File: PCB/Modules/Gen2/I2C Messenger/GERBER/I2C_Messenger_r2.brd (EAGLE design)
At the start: 40.2 x 83 mm, 17 parts, among them IC1 SN65HVD31DR, IC2 LM3480-5.0

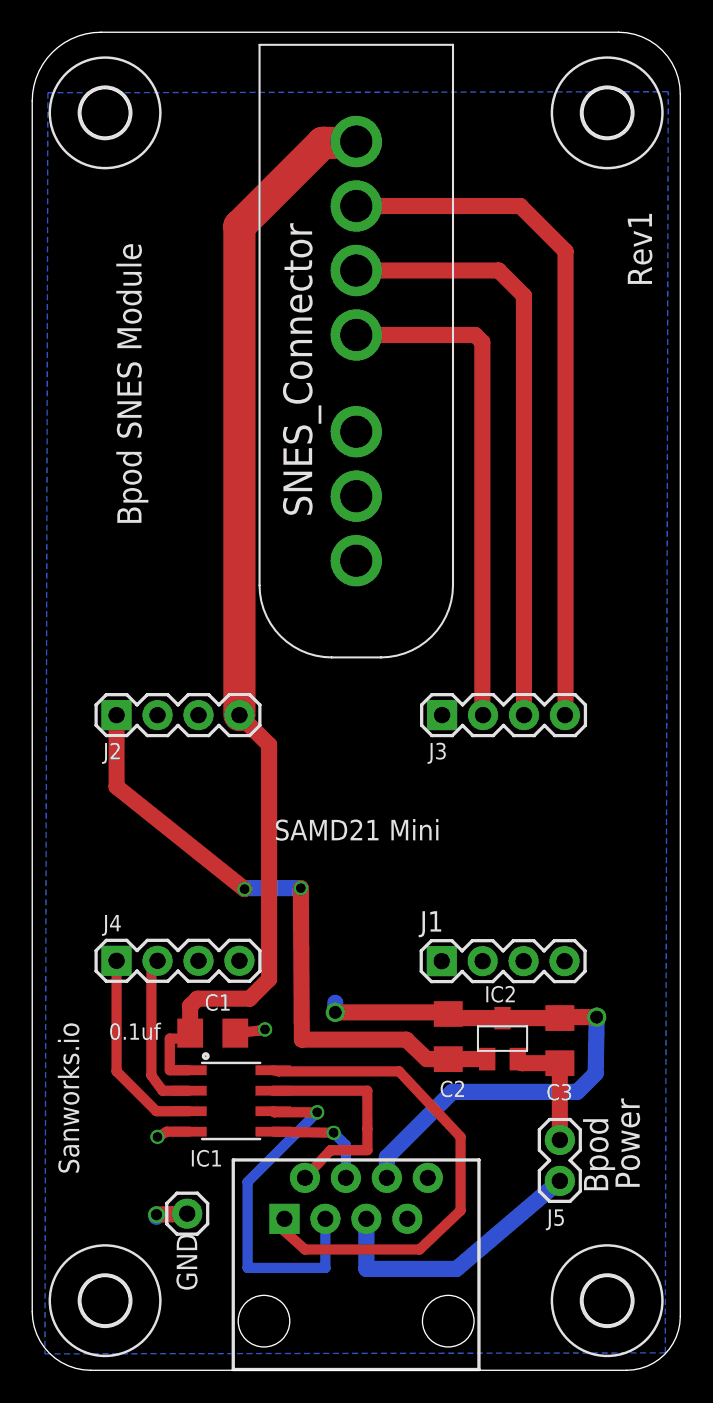
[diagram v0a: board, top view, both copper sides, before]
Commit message: -Critical Update for modules with optional RJ45 power (ValveDriver, I2C, SNES and DDS); new PCB designs add a diode to prevent USB power from entering output pin of 5V regulator, when RJ45 (state machine) power is not connected. This update greatly reduces unnecessary power consumption and heat dissipation. If you built a board using the previous designs, please Email a photo of your board to Sanworks support for a free upgrade. -Updated component names on some boards and on web BOMs to avoid skipping parts -Renamed Gen2 module PCB folder from '0.7' to 'Gen2' -Retired pocket state machine (to be replaced with Bpod State Machine r1)
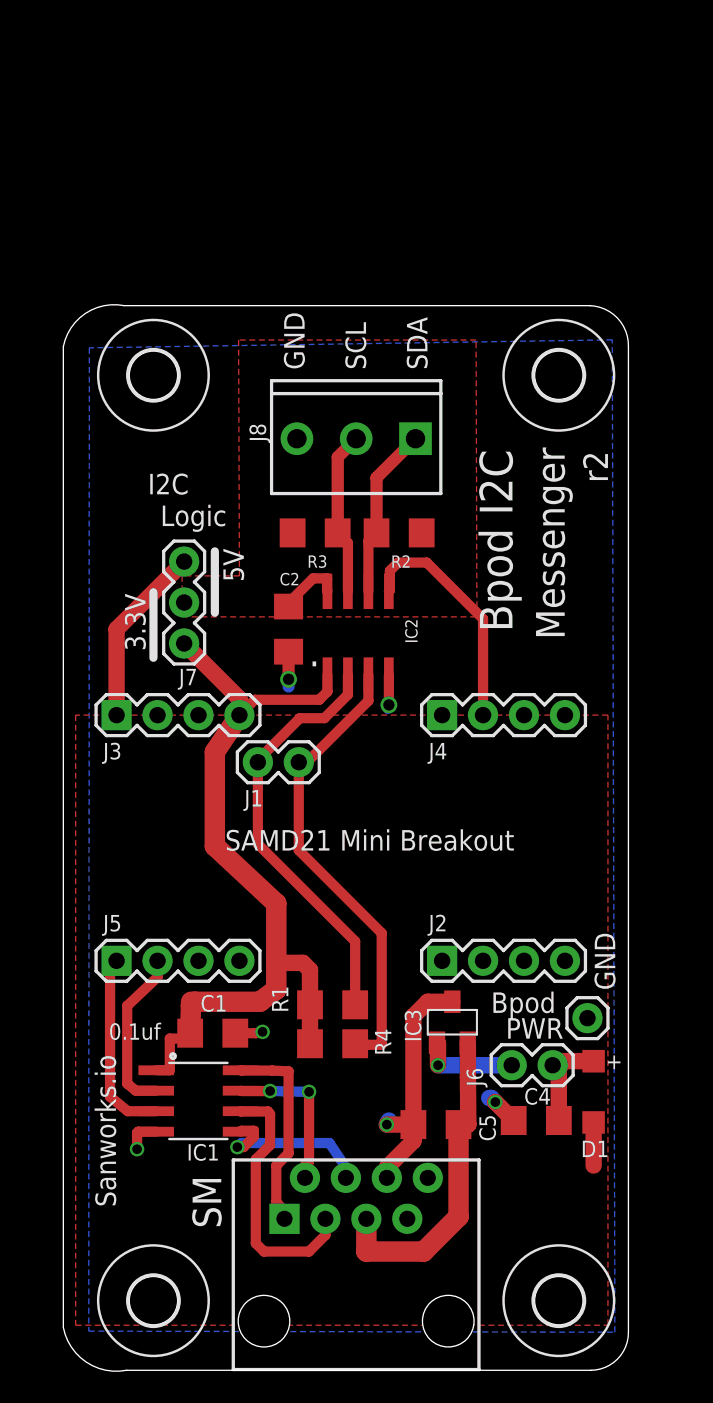
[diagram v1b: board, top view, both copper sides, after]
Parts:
- removed C3: 0.1uf, SparkFun-Capacitors:1206
- removed U$2: SNES_CONNECTOR, JoshParts10:SNES_CONNECTOR
- added C4, C5: 0.1uf, SparkFun-Capacitors:1206
- added D1: MBR0520LT, diode:SOD123
- added IC3: LM3480-5.0, regulators:SOT-23-3
- added J6: (no value), SparkFun-Connectors:1X02
- added J8: (no value), SparkFun-Connectors:SCREWTERMINAL-3.5MM-3_LOCK.007S
- added JG: (no value), SparkFun-Connectors:1X01
- added R1, R2, R3, R4: 10k, SparkFun-Resistors:1206
- IC2: value LM3480-5.0 -> PCA9517; device regulators:SOT-23-3 -> PCA9517:SO-08
- J1: device SparkFun-Connectors:1X04 -> SparkFun-Connectors:1X02@1
- J5: device SparkFun-Connectors:1X02 -> SparkFun-Connectors:1X04
- J7: device SparkFun-Connectors:1X01 -> SparkFun-Connectors:1X03
- moved J7 35.4 mm to (6.22, 45.1), turned to 90 degrees
- moved J5 29.7 mm to (2.03, 25.4), turned to 0 degrees
- moved C2 27.1 mm to (12.7, 46.0)
- moved IC2 26.7 mm to (17.0, 45.7)
- moved J2 25.3 mm to (22.2, 25.4)
- moved J4 25.3 mm to (22.2, 40.6)
- moved J3 20.2 mm to (2.03, 40.6)
- moved J1 16.8 mm to (10.8, 37.7)
- moved H3 16.6 mm to (29.5, 61.7)
- moved H4 16.6 mm to (4.32, 61.7)
- moved H2 3.00 mm to (29.5, 4.32)
- moved H1 3.00 mm to (4.32, 4.32)
- moved IC1 2.03 mm to (7.11, 16.7)
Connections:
- removed net N$24: J5.2, U$1.5
- removed net N$3: J3.4, U$2.CLOCK
- new net N$11: IC2.3, J1.2, R4.1
- new net N$12: C2.1, IC2.8, J7.2, R2.2, R3.2
- new net N$13: IC2.5, J4.2
- new net N$14: IC2.6, J8.1, R2.1
- new net N$15: IC2.7, J8.2, R3.1
- new net N$5: IC2.2, J1.1, R1.1
- net 5V: now also D1.C, J3.1, J7.3; no longer C2.2, IC2.1, J2.1
- net GND: now also C2.2, C4.1, C5.1, IC2.4, IC3.3, J5.4, J8.3, JG.1; no longer C2.1, C3.1, IC2.3, J4.4, J7.1, U$2.GND
- net N$1: now also C4.2, D1.A, J6.2; no longer J3.2, U$2.DATA
- net N$2: now also IC3.1, J6.1; no longer J3.3, U$2.LATCH
- net N$26: now also C5.2, IC3.2, U$1.5; no longer C3.2, IC2.2, J5.1
- net N$4: now also J5.1; no longer J4.1
- net N$6: now also J5.2; no longer J4.2
- net VCC: now also IC2.1, J3.4, J7.1, R1.2, R4.2; no longer J2.4, U$2.V+
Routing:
- net N$3: track 42.9 -> 0.00 mm
- net N$2: track 37.1 -> 6.00 mm, vias 0 -> 1
- net N$11: track 0.00 -> 29.0 mm
- net N$5: track 0.00 -> 26.2 mm
- net 5V: track 39.5 -> 13.9 mm, vias 2 -> 0
- net N$1: track 31.2 -> 6.61 mm
- net VCC: track 70.1 -> 50.9 mm
- net N$7: track 31.0 -> 12.7 mm
- net GND: track 43.0 -> 25.7 mm, vias 5 -> 6
- net N$24: track 17.1 -> 0.00 mm
- net N$13: track 0.00 -> 14.7 mm
- net N$26: track 7.47 -> 20.0 mm
- net N$14: track 0.00 -> 10.7 mm
- net N$15: track 0.00 -> 10.2 mm
- net N$9: track 22.1 -> 16.3 mm, vias 1 -> 0
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- added copper zone on layer 1, net 5V
- added copper zone on layer 1, net N$12
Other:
- board size 40.2 x 83 mm -> 35.1 x 66.1 mm
- board text added: "+"
- board text added: "."
- board text added: "3.3V"
- board text added: "5V"
- board text added: "Bpod I2C"
- board text added: "I2C"
- board text added: "Logic"
- board text added: "Messenger"
- board text added: "PWR"
- board text added: "SAMD21 Mini Breakout"
- board text added: "SCL"
- board text added: "SDA"
- board text added: "SM"
- board text added: "r2"
- board text removed: "Bpod SNES Module"
- board text removed: "Power"
- board text removed: "Rev1"
- board text removed: "SAMD21 Mini"
- board text removed: "SNES_Connector"
